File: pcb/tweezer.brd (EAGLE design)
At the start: 20 x 26 mm, 33 parts, among them IC1 AD7995, IC2 TS507CLT, IC3 TS507CLT, IC5 ESDA6V1SC5, IC6 AT24CS04-SOT23

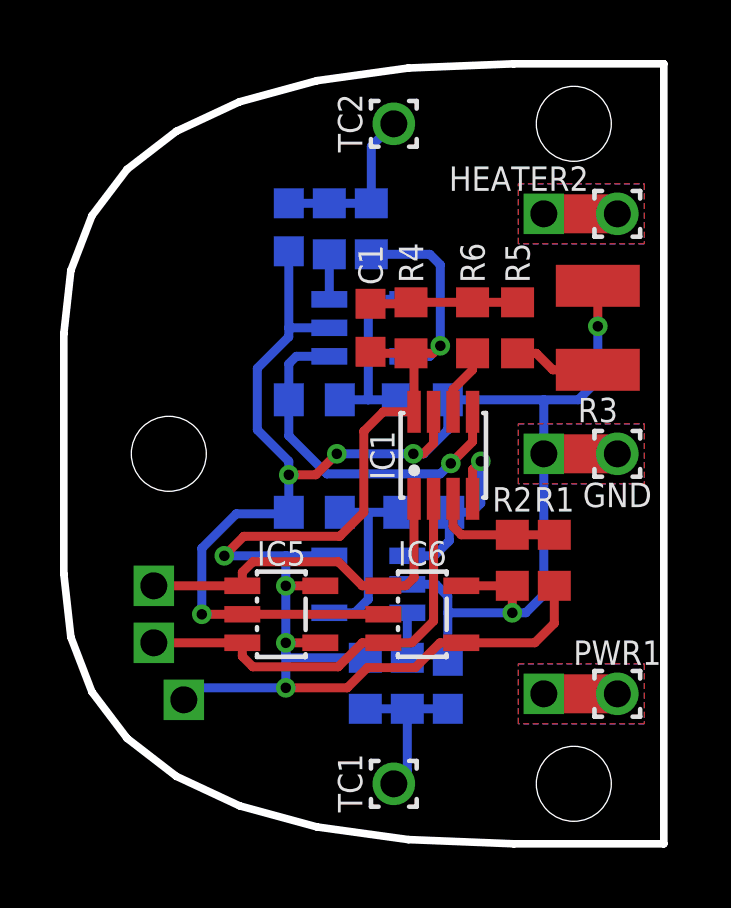
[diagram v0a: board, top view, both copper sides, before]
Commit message: shottky diode added to iron/tweezer
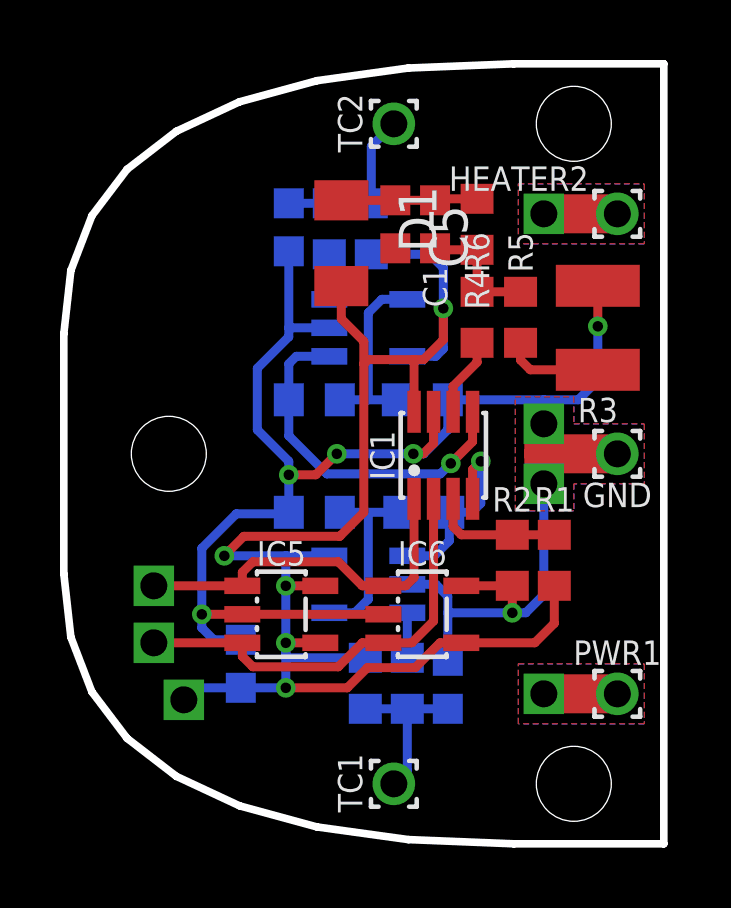
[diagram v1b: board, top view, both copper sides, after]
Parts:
- added C4, C5: 1µF, common:C0603
- added D1: BAT54H, solderpi:SOD123-F
- added U$1: WIREPAD, solderpi:WIREPAD
- R1: value 20k 0,1% -> 1k
- R2: value 68k @25°C, 1%, ß=3985 K -> 1k @25°C, 1%, ß=3985 K
- R4: value 5,1M -> 4M7
- R5: value 1k -> 100k
- moved R4 4.09 mm to (13.8, 20.6), turned to 90 degrees
- moved C1 4.07 mm to (12.4, 20.6), turned to 270 degrees
- moved U$11 1.00 mm to (16.0, 14.0)
- moved R6 0.38 mm to (13.8, 17.6)
- moved R5 0.36 mm to (15.2, 17.6)
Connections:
- new net N$1: C1.1, C5.1, D1.1, R4.2
- net +5V: now also C4.1, D1.2; no longer C1.1, R4.2
- net GND: now also C4.2, C5.2, U$1.1
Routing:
- net +5V: track 48.7 -> 53.5 mm
- net N$1: track 0.00 -> 4.58 mm
- net GND: track 58.4 -> 62.4 mm
- net MOTION_FIL: track 4.92 -> 4.30 mm

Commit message: iron tweezer updated
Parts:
- R10, R11, R14, R7: value 2k -> 2k 0.1%
- R12, R13, R8, R9: value 1M -> 1M 0,1%

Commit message: boms reworked
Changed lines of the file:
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@@
 <?xml version="1.0" encoding="utf-8"?>
 <!DOCTYPE eagle SYSTEM "eagle.dtd">
-<eagle version="9.4.2">
+<eagle version="9.5.0">
 <drawing>
 <settings>
@@
 <layer number="14" name="Route14" color="1" fill="6" visible="no" active="no"/>
 <layer number="15" name="Route15" color="4" fill="6" visible="no" active="no"/>
-<layer number="16" name="Bottom" color="1" fill="1" visible="yes" active="yes"/>
+<layer number="16" name="Bottom" color="1" fill="1" visible="no" active="yes"/>
 <layer number="17" name="Pads" color="2" fill="1" visible="yes" active="yes"/>
 <layer number="18" name="Vias" color="2" fill="1" visible="yes" active="yes"/>
@@
 <layer number="20" name="Dimension" color="24" fill="1" visible="yes" active="yes"/>
 <layer number="21" name="tPlace" color="7" fill="1" visible="yes" active="yes"/>
-<layer number="22" name="bPlace" color="7" fill="1" visible="yes" active="yes"/>
+<layer number="22" name="bPlace" color="7" fill="1" visible="no" active="yes"/>
 <layer number="23" name="tOrigins" color="15" fill="1" visible="yes" active="yes"/>
-<layer number="24" name="bOrigins" color="15" fill="1" visible="yes" active="yes"/>
-<layer number="25" name="tNames" color="7" fill="1" visible="no" active="yes"/>
+<layer number="24" name="bOrigins" color="15" fill="1" visible="no" active="yes"/>
+<layer number="25" name="tNames" color="7" fill="1" visible="yes" active="yes"/>
 <layer number="26" name="bNames" color="7" fill="1" visible="no" active="yes"/>
 <layer number="27" name="tValues" color="7" fill="1" visible="no" active="yes"/>
@@
 <layer number="38" name="bTest" color="7" fill="1" visible="no" active="yes"/>
 <layer number="39" name="tKeepout" color="4" fill="11" visible="yes" active="yes"/>
-<layer number="40" name="bKeepout" color="1" fill="11" visible="yes" active="yes"/>
-<layer number="41" name="tRestrict" color="4" fill="10" visible="no" active="yes"/>
+<layer number="40" name="bKeepout" color="1" fill="11" visible="no" active="yes"/>
+<layer number="41" name="tRestrict" color="4" fill="10" visible="yes" active="yes"/>
 <layer number="42" name="bRestrict" color="1" fill="10" visible="no" active="yes"/>
-<layer number="43" name="vRestrict" color="2" fill="10" visible="no" active="yes"/>
+<layer number="43" name="vRestrict" color="2" fill="10" visible="yes" active="yes"/>
 <layer number="44" name="Drills" color="7" fill="1" visible="no" active="yes"/>
 <layer number="45" name="Holes" color="7" fill="1" visible="yes" active="yes"/>
@@
 </element>
 <element name="D1" library="solderpi" library_urn="urn:adsk.eagle:library:1437534" package="SOD123-F" package3d_urn="urn:adsk.eagle:package:1609183/2" value="BAT54H" x="9.25" y="20.02" smashed="yes" rot="R270">
-<attribute name="NAME" x="11.155" y="21.925" size="1.27" layer="25" rot="R270"/>
+<attribute name="NAME" x="9.25" y="17.0216" size="0.8128" layer="25" rot="R90" align="center-right"/>
 <attribute name="OC_DIGIKEY" value="1727-3569-1-ND" x="9.25" y="20.02" size="1.778" layer="27" rot="R270" display="off"/>
 <attribute name="VALUE" x="6.075" y="21.925" size="1.27" layer="27" rot="R270"/>
 </element>
 <element name="C4" library="common" library_urn="urn:adsk.eagle:library:8241912" package="C0603" package3d_urn="urn:adsk.eagle:package:8241929/3" value="1µF" x="5.9" y="6" smashed="yes" rot="MR90">
-<attribute name="NAME" x="7.035" y="5.365" size="1.27" layer="26" rot="MR90"/>
+<attribute name="NAME" x="5.9" y="4.5746" size="0.8128" layer="26" rot="MR90" align="center-right"/>
 <attribute name="OC_DIGIKEY" value="1276-1034-1-ND" x="5.9" y="6" size="1.778" layer="28" rot="MR90" display="off"/>
 <attribute name="VALUE" x="3.695" y="5.365" size="1.27" layer="28" rot="MR90"/>
 </element>
 <element name="C5" library="common" library_urn="urn:adsk.eagle:library:8241912" package="C0603" package3d_urn="urn:adsk.eagle:package:8241929/3" value="1µF" x="11.05" y="20.65" smashed="yes" rot="R270">
-<attribute name="NAME" x="12.185" y="21.285" size="1.27" layer="25" rot="R270"/>
+<attribute name="NAME" x="11.05" y="19.2246" size="0.8128" layer="25" rot="R90" align="center-right"/>
 <attribute name="OC_DIGIKEY" value="1276-1034-1-ND" x="11.05" y="20.65" size="1.778" layer="27" rot="R270" display="off"/>
 <attribute name="VALUE" x="8.845" y="21.285" size="1.27" layer="27" rot="R270"/>
